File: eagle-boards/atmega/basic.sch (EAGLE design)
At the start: 7 parts, among them IC1 ATMEGA168-20P, Q1 BC547

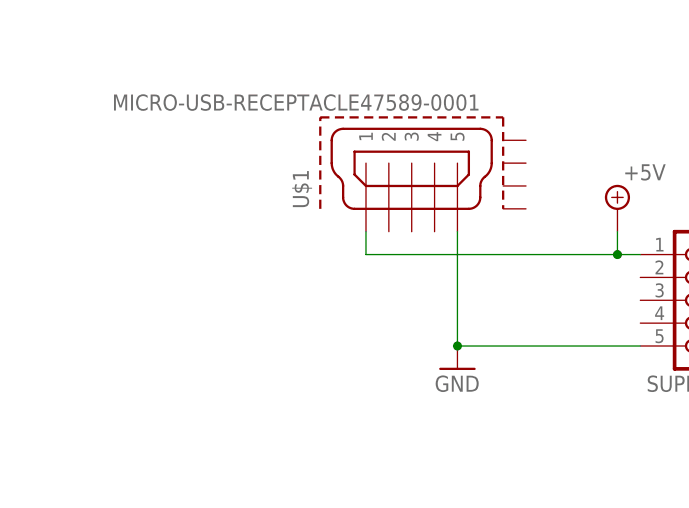
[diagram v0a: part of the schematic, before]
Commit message: Re-layout board to align with actuator.
Also update the microUSB connector to a SnapEDA symbol for an Amphenol connector that appears to be easier to source and solder.
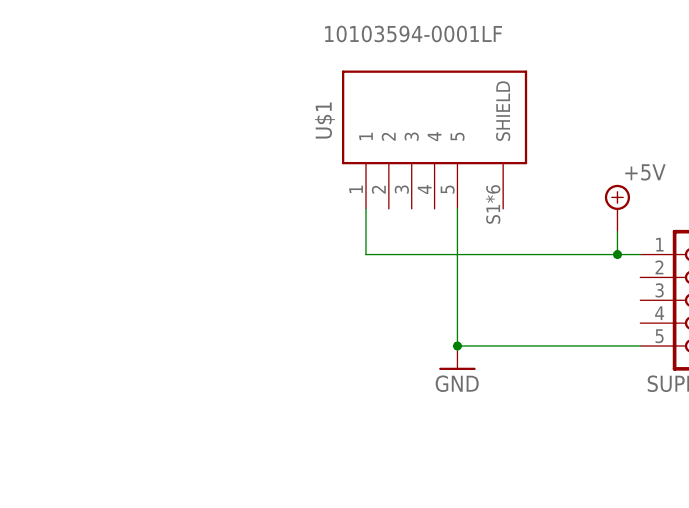
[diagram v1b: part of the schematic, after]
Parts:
- U$1: value MICRO-USB-RECEPTACLE47589-0001 -> 10103594-0001LF; device con-molex-usb:MICRO-USB-RECEPTACLE47589-0001 -> 10103594-0001LF:10103594-0001LF
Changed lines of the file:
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@@
 </classes>
 <parts>
-<part name="U$1" library="con-molex-usb" deviceset="MICRO-USB-RECEPTACLE" device="47589-0001"/>
+<part name="U$1" library="10103594-0001LF" deviceset="10103594-0001LF" device=""/>
 <part name="MCU" library="con-lsta" library_urn="urn:adsk.eagle:library:161" deviceset="FE20-1" device="" package3d_urn="urn:adsk.eagle:package:8196/1"/>
 <part name="SUPPLY" library="con-lsta" library_urn="urn:adsk.eagle:library:161" deviceset="FE05-1" device="" package3d_urn="urn:adsk.eagle:package:8190/1"/>
@@
 </plain>
 <instances>
-<instance part="U$1" gate="G$1" x="-96.52" y="99.06" smashed="yes" rot="R90">
-<attribute name="NAME" x="-107.95" y="96.52" size="1.778" layer="95" font="vector" rot="R90"/>
-<attribute name="VALUE" x="-88.9" y="109.22" size="1.778" layer="96" font="vector" rot="R180"/>
+<instance part="U$1" gate="G$1" x="-93.98" y="106.68" smashed="yes" rot="R90">
+<attribute name="NAME" x="-105.41" y="104.14" size="1.778" layer="95" font="vector" rot="R90"/>
+<attribute name="VALUE" x="-86.36" y="116.84" size="1.778" layer="96" font="vector" rot="R180"/>
 </instance>
 <instance part="MCU" gate="G$1" x="120.65" y="39.37" smashed="yes" rot="R180">
@@
 <pinref part="SUPPLY" gate="G$1" pin="5"/>
 <pinref part="U$1" gate="G$1" pin="5"/>
-<wire x1="-91.44" y1="93.98" x2="-91.44" y2="81.28" width="0.1524" layer="91"/>
+<wire x1="-91.44" y1="96.52" x2="-91.44" y2="81.28" width="0.1524" layer="91"/>
 <wire x1="-91.44" y1="81.28" x2="-71.12" y2="81.28" width="0.1524" layer="91"/>
 <pinref part="GND1" gate="1" pin="GND"/>
@@
 <wire x1="-73.66" y1="91.44" x2="-73.66" y2="93.98" width="0.1524" layer="91"/>
 <pinref part="U$1" gate="G$1" pin="1"/>
-<wire x1="-101.6" y1="93.98" x2="-101.6" y2="91.44" width="0.1524" layer="91"/>
+<wire x1="-101.6" y1="96.52" x2="-101.6" y2="91.44" width="0.1524" layer="91"/>
 <wire x1="-101.6" y1="91.44" x2="-73.66" y2="91.44" width="0.1524" layer="91"/>
 <junction x="-73.66" y="91.44"/>
